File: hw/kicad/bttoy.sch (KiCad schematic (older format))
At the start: 35 parts

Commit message: - more schematic work
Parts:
- gave numbers to parts that had none: 35
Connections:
- net GND: now also R5.2, R6.2, R7.2
- net dgb_led1: now reaches U4.17 (PTB1)
- net dgb_led1: now also D3.1 (K)
- net dbg_led2: now reaches U4.18 (PTB2)
- net dbg_led2: now also D4.1 (K)
- net dbg_led3: now reaches U4.19 (PTA8)
- net dbg_led3: now also D5.1 (K)
- no-connect marks 36 -> 56
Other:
- moved on the sheet: D3, D4, D5, R5, R6, R7, U4

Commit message: - start layout
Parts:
- C1, C4, C5, C6, C7, R1, R2, R3, R4, R5, R6, R7: footprint (none) -> kicadlib:SMD_0603_R
- C2: footprint (none) -> kicadlib:SMD_5X5.2_CAP
- C3: footprint (none) -> kicadlib:SMD_0805_R
- D1: footprint (none) -> kicadlib:SMD_1206_DIODE
- D2, D3, D4, D5: footprint (none) -> kicadlib:SMD_0603_LED
- J1: footprint (none) -> kicadlib:usb_micro_b_smt
- J2: footprint (none) -> kicadlib:HC-07_bluetooth
- J3: footprint (none) -> kicadlib:ARM_10_PIN_SMT
- JP1: footprint (none) -> kicadlib:jmp_small
- L1: footprint (none) -> kicadlib:SMD_4x4_INDUCTOR
- P1, P2, P3, P4, P5: footprint (none) -> kicadlib:TEST_0.100
- SW1: footprint (none) -> kicadlib:TH_APEM_MHSS1105_SPDT
- U1, U2, U3: footprint (none) -> kicadlib:SMD_SOT23-5
- U4: footprint (none) -> kicadlib:SMD_LQFP-32
- U5: footprint (none) -> kicadlib:SMD_SOIC-10NB
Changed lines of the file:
@@
 F 0 "U4" H 6500 2450 60  0000 C CNN
 F 1 "MKL05Z32VLC4" H 6550 2300 60  0000 C CNN
-F 2 "" H 6100 2250 60  0000 C CNN
+F 2 "kicadlib:SMD_LQFP-32" H 6100 2250 60  0001 C CNN
 F 3 "" H 6100 2250 60  0000 C CNN
 	1    6100 2250
@@
 F 0 "U3" H 5350 4000 60  0000 C CNN
 F 1 "MCP73831" H 5350 4600 60  0000 C CNN
-F 2 "" H 5350 4300 60  0000 C CNN
+F 2 "kicadlib:SMD_SOT23-5" H 5350 4300 60  0001 C CNN
 F 3 "" H 5350 4300 60  0000 C CNN
 	1    5350 4300
@@
 F 0 "J1" H 1100 600 60  0000 C CNN
 F 1 "USB-micro-b" H 1100 1850 60  0000 C CNN
-F 2 "" H 1100 1200 60  0000 C CNN
+F 2 "kicadlib:usb_micro_b_smt" H 1100 1200 60  0001 C CNN
 F 3 "" H 1100 1200 60  0000 C CNN
 	1    1100 1200
@@
 F 0 "U1" H 1900 4250 60  0000 C CNN
 F 1 "AAT3221/MIC5504" H 1900 4850 60  0000 C CNN
-F 2 "" H 1900 4450 60  0000 C CNN
+F 2 "kicadlib:SMD_SOT23-5" H 1900 4450 60  0001 C CNN
 F 3 "" H 1900 4450 60  0000 C CNN
 	1    1900 4450
@@
 F 0 "R3" V 4630 4950 40  0000 C CNN
 F 1 "1K" V 4557 4951 40  0000 C CNN
-F 2 "" V 4480 4950 30  0000 C CNN
+F 2 "kicadlib:SMD_0603_R" V 4480 4950 30  0001 C CNN
 F 3 "" H 4550 4950 30  0000 C CNN
 	1    4550 4950
@@
 F 0 "C6" H 4250 4450 40  0000 L CNN
 F 1 "4.7uF" H 4256 4265 40  0000 L CNN
-F 2 "" H 4288 4200 30  0000 C CNN
+F 2 "kicadlib:SMD_0603_R" H 4288 4200 30  0001 C CNN
 F 3 "" H 4250 4350 60  0000 C CNN
 	1    4250 4350
@@
 F 0 "D2" H 4550 4450 50  0000 C CNN
 F 1 "LED" H 4550 4250 50  0000 C CNN
-F 2 "" H 4550 4350 60  0000 C CNN
+F 2 "kicadlib:SMD_0603_LED" H 4550 4350 60  0001 C CNN
 F 3 "" H 4550 4350 60  0000 C CNN
 	1    4550 4350
@@
 F 0 "R4" V 6180 4550 40  0000 C CNN
 F 1 "2K" V 6107 4551 40  0000 C CNN
-F 2 "" V 6030 4550 30  0000 C CNN
+F 2 "kicadlib:SMD_0603_R" V 6030 4550 30  0001 C CNN
 F 3 "" H 6100 4550 30  0000 C CNN
 	1    6100 4550
@@
 F 0 "C7" H 6350 4450 40  0000 L CNN
 F 1 "4.7uF" H 6356 4265 40  0000 L CNN
-F 2 "" H 6388 4200 30  0000 C CNN
+F 2 "kicadlib:SMD_0603_R" H 6388 4200 30  0001 C CNN
 F 3 "" H 6350 4350 60  0000 C CNN
 	1    6350 4350
@@
 F 0 "C1" H 1050 4500 40  0000 L CNN
 F 1 "1uF" H 1056 4315 40  0000 L CNN
-F 2 "" H 1088 4250 30  0000 C CNN
+F 2 "kicadlib:SMD_0603_R" H 1088 4250 30  0001 C CNN
 F 3 "" H 1050 4400 60  0000 C CNN
 	1    1050 4400
@@
 F 0 "C4" H 2750 4500 40  0000 L CNN
 F 1 "1uF" H 2756 4315 40  0000 L CNN
-F 2 "" H 2788 4250 30  0000 C CNN
+F 2 "kicadlib:SMD_0603_R" H 2788 4250 30  0001 C CNN
 F 3 "" H 2750 4400 60  0000 C CNN
 	1    2750 4400
@@
 F 0 "J3" H 9650 450 60  0000 C CNN
 F 1 "ARM_10PIN" H 9650 2100 60  0000 C CNN
-F 2 "" H 9650 1450 60  0000 C CNN
+F 2 "kicadlib:ARM_10_PIN_SMT" H 9650 1450 60  0001 C CNN
 F 3 "" H 9650 1450 60  0000 C CNN
 	1    9650 1450
@@
 F 0 "J2" H 4200 -550 60  0000 C CNN
 F 1 "HC-07_BLUETOOTH" H 3350 1850 60  0000 C CNN
-F 2 "" H 2550 1450 60  0000 C CNN
+F 2 "kicadlib:HC-07_bluetooth" H 2550 1450 60  0001 C CNN
 F 3 "" H 2550 1450 60  0000 C CNN
 	1    2550 1450
@@
 F 0 "U2" H 3000 6350 60  0000 C CNN
 F 1 "MIC2288" H 3000 6950 60  0000 C CNN
-F 2 "" H 3000 6600 60  0000 C CNN
+F 2 "kicadlib:SMD_SOT23-5" H 3000 6600 60  0001 C CNN
 F 3 "" H 3000 6600 60  0000 C CNN
 	1    3000 6650
@@
 F 0 "L1" V 2900 6050 40  0000 C CNN
 F 1 "10uH/650mA (LQH43CN100K03)" V 3100 5600 40  0000 C CNN
-F 2 "" H 2950 6050 60  0000 C CNN
+F 2 "kicadlib:SMD_4x4_INDUCTOR" H 2950 6050 60  0001 C CNN
 F 3 "" H 2950 6050 60  0000 C CNN
 	1    2950 6050
@@
 F 0 "C5" H 3650 6900 40  0000 L CNN
 F 1 "2.2uF/10V" H 3656 6715 40  0000 L CNN
-F 2 "" H 3688 6650 30  0000 C CNN
+F 2 "kicadlib:SMD_0603_R" H 3688 6650 30  0001 C CNN
 F 3 "" H 3650 6800 60  0000 C CNN
 	1    3650 6800
@@
 F 0 "C3" H 1800 6250 40  0000 L CNN
 F 1 "10uF/16V" H 1600 6450 40  0000 L CNN
-F 2 "" H 1788 6200 30  0000 C CNN
+F 2 "kicadlib:SMD_0805_R" H 1788 6200 30  0001 C CNN
 F 3 "" H 1750 6350 60  0000 C CNN
 	1    1750 6350
@@
 F 0 "D1" H 2350 6150 40  0000 C CNN
 F 1 "40v/1A" H 2350 5950 40  0000 C CNN
-F 2 "" H 2350 6050 60  0000 C CNN
+F 2 "kicadlib:SMD_1206_DIODE" H 2350 6050 60  0001 C CNN
 F 3 "" H 2350 6050 60  0000 C CNN
 	1    2350 6050
@@
 F 0 "R1" V 2130 6500 40  0000 C CNN
 F 1 "6.2K" V 2057 6501 40  0000 C CNN
-F 2 "" V 1980 6500 30  0000 C CNN
+F 2 "kicadlib:SMD_0603_R" V 1980 6500 30  0001 C CNN
 F 3 "" H 2050 6500 30  0000 C CNN
 	1    2050 6500
@@
 F 0 "R2" V 2130 7100 40  0000 C CNN
 F 1 "1K" V 2057 7101 40  0000 C CNN
-F 2 "" V 1980 7100 30  0000 C CNN
+F 2 "kicadlib:SMD_0603_R" V 1980 7100 30  0001 C CNN
 F 3 "" H 2050 7100 30  0000 C CNN
 	1    2050 7100
@@
 F 0 "JP1" H 3050 7600 60  0000 C CNN
 F 1 "MPS ENABLE" H 3050 7370 40  0000 C CNN
-F 2 "" H 3050 7450 60  0000 C CNN
+F 2 "kicadlib:jmp_small" H 3050 7450 60  0001 C CNN
 F 3 "" H 3050 7450 60  0000 C CNN
 	1    3050 7450
@@
 F 0 "SW1" H 6900 4300 50  0000 C CNN
 F 1 "SPDT (Apem MHSS1105)" H 7200 3900 50  0000 C CNN
-F 2 "" H 7100 4150 60  0000 C CNN
+F 2 "kicadlib:TH_APEM_MHSS1105_SPDT" H 7100 4150 60  0001 C CNN
 F 3 "" H 7100 4150 60  0000 C CNN
 	1    7100 4150
@@
 F 0 "C2" H 1200 6450 50  0000 L CNN
 F 1 "30uF" H 1150 6250 50  0000 L CNN
-F 2 "" H 1150 6350 60  0000 C CNN
+F 2 "kicadlib:SMD_5X5.2_CAP" H 1150 6350 60  0001 C CNN
 F 3 "" H 1150 6350 60  0000 C CNN
 	1    1150 6350
@@
 F 0 "U5" H 6900 5600 60  0000 C CNN
 F 1 "LV8548" H 6900 6400 60  0000 C CNN
-F 2 "" H 6800 6050 60  0000 C CNN
+F 2 "kicadlib:SMD_SOIC-10NB" H 6800 6050 60  0001 C CNN
 F 3 "" H 6800 6050 60  0000 C CNN
 	1    6900 6050
@@
 F 0 "P2" H 7650 5850 40  0000 C CNN
 F 1 "M1+" H 7650 5800 30  0000 C CNN
-F 2 "" H 7650 5550 60  0000 C CNN
+F 2 "kicadlib:TEST_0.100" H 7650 5550 60  0001 C CNN
 F 3 "" H 7650 5550 60  0000 C CNN
 	1    7650 5550
@@
 F 0 "P3" H 7650 6250 40  0000 C CNN
 F 1 "M1-" H 7650 6200 30  0000 C CNN
-F 2 "" H 7650 5950 60  0000 C CNN
+F 2 "kicadlib:TEST_0.100" H 7650 5950 60  0001 C CNN
 F 3 "" H 7650 5950 60  0000 C CNN
 	1    7650 5950
@@
 F 0 "P4" H 8400 6350 40  0000 C CNN
 F 1 "M2+" H 8400 6300 30  0000 C CNN
-F 2 "" H 8400 6050 60  0000 C CNN
+F 2 "kicadlib:TEST_0.100" H 8400 6050 60  0001 C CNN
 F 3 "" H 8400 6050 60  0000 C CNN
 	1    8400 6050
@@
 F 0 "P5" H 8400 6750 40  0000 C CNN
 F 1 "M2-" H 8400 6700 30  0000 C CNN
-F 2 "" H 8400 6450 60  0000 C CNN
+F 2 "kicadlib:TEST_0.100" H 8400 6450 60  0001 C CNN
 F 3 "" H 8400 6450 60  0000 C CNN
 	1    8400 6450
@@
 F 0 "P1" H 1150 6200 40  0000 C CNN
 F 1 "+9V_DBG" H 1150 6150 30  0000 C CNN
-F 2 "" H 1150 5900 60  0000 C CNN
+F 2 "kicadlib:TEST_0.100" H 1150 5900 60  0001 C CNN
 F 3 "" H 1150 5900 60  0000 C CNN
 	1    1150 5900
@@
 F 0 "D3" H 8700 4000 50  0000 C CNN
 F 1 "LED" H 8700 3800 50  0000 C CNN
-F 2 "" H 8700 3900 60  0000 C CNN
+F 2 "kicadlib:SMD_0603_LED" H 8700 3900 60  0001 C CNN
 F 3 "" H 8700 3900 60  0000 C CNN
 	1    8700 3900
@@
 F 0 "R5" V 8780 4450 40  0000 C CNN
 F 1 "1K" V 8707 4451 40  0000 C CNN
-F 2 "" V 8630 4450 30  0000 C CNN
+F 2 "kicadlib:SMD_0603_R" V 8630 4450 30  0001 C CNN
 F 3 "" H 8700 4450 30  0000 C CNN
 	1    8700 4450
@@
 F 0 "D4" H 9050 4000 50  0000 C CNN
 F 1 "LED" H 9050 3800 50  0000 C CNN
-F 2 "" H 9050 3900 60  0000 C CNN
+F 2 "kicadlib:SMD_0603_LED" H 9050 3900 60  0001 C CNN
 F 3 "" H 9050 3900 60  0000 C CNN
 	1    9050 3900
@@
 F 0 "R6" V 9130 4450 40  0000 C CNN
 F 1 "1K" V 9057 4451 40  0000 C CNN
-F 2 "" V 8980 4450 30  0000 C CNN
+F 2 "kicadlib:SMD_0603_R" V 8980 4450 30  0001 C CNN
 F 3 "" H 9050 4450 30  0000 C CNN
 	1    9050 4450
@@
 F 0 "D5" H 9400 4000 50  0000 C CNN
 F 1 "LED" H 9400 3800 50  0000 C CNN
-F 2 "" H 9400 3900 60  0000 C CNN
+F 2 "kicadlib:SMD_0603_LED" H 9400 3900 60  0001 C CNN
 F 3 "" H 9400 3900 60  0000 C CNN
 	1    9400 3900
@@
 F 0 "R7" V 9480 4450 40  0000 C CNN
 F 1 "1K" V 9407 4451 40  0000 C CNN
-F 2 "" V 9330 4450 30  0000 C CNN
+F 2 "kicadlib:SMD_0603_R" V 9330 4450 30  0001 C CNN
 F 3 "" H 9400 4450 30  0000 C CNN
 	1    9400 4450

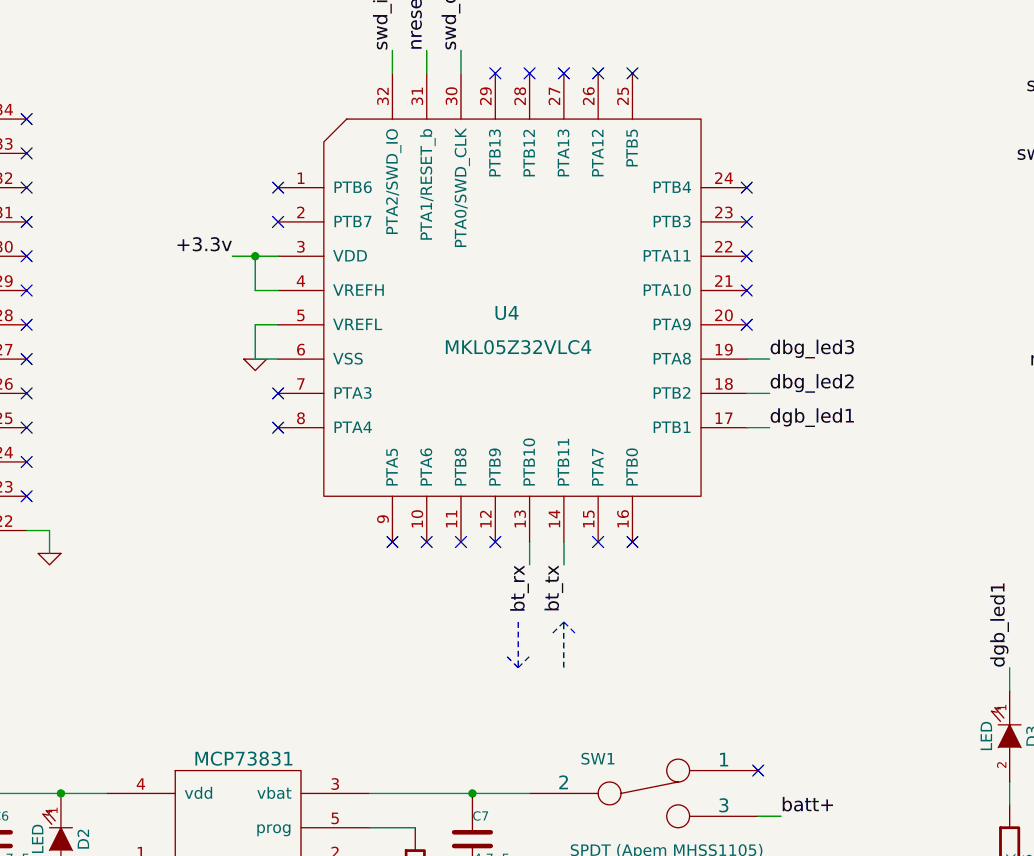
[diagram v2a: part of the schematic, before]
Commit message: - connect motor control signals
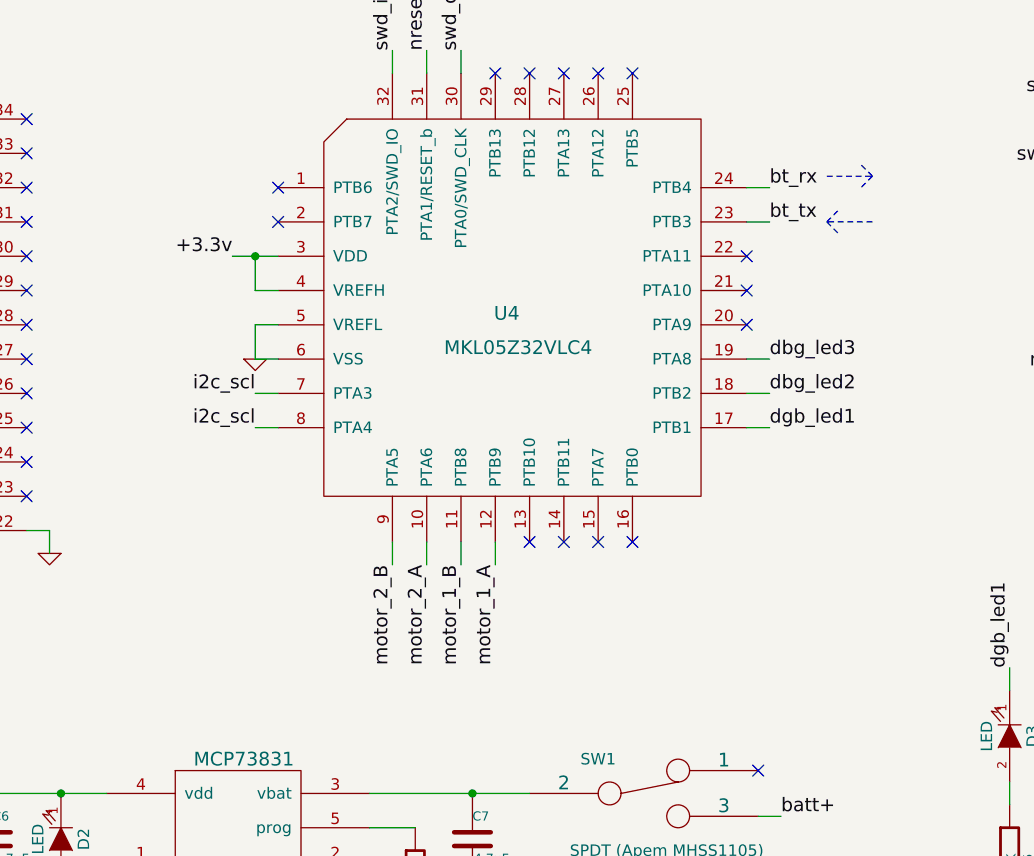
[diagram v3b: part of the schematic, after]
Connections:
- net bt_rx: now also U4.24 (PTB4); no longer U4.13 (PTB10)
- net bt_tx: now also U4.23 (PTB3); no longer U4.14 (PTB11)
- net motor_1_A: now also U4.12 (PTB9)
- net motor_1_B: now also U4.11 (PTB8)
- net motor_2_A: now also U4.10 (PTA6)
- net motor_2_B: now also U4.9 (PTA5)
- net i2c_scl: now reaches U4.7 (PTA3)
- net i2c_scl: now also U4.8 (PTA4)
- no-connect marks 56 -> 50
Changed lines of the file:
@@
 Text Label 2250 1200 2    60   ~ 0
 bt_tx
-Text Label 6600 3150 3    60   ~ 0
+Text Label 7650 1500 0    60   ~ 0
 bt_rx
-Text Label 6750 3150 3    60   ~ 0
+Text Label 7650 1650 0    60   ~ 0
 bt_tx
 Text Label 6300 5950 2    60   ~ 0
@@
 Connection ~ 5400 1800
 Wire Notes Line
-	6550 3400 6550 3600
-Wire Notes Line
-	6550 3600 6600 3550
-Wire Notes Line
-	6550 3600 6500 3550
-Wire Wire Line
-	6600 3150 6600 3050
-Wire Notes Line
-	6750 3600 6750 3400
-Wire Notes Line
-	6750 3400 6700 3450
-Wire Notes Line
-	6750 3400 6800 3450
-Wire Wire Line
-	6750 3150 6750 3050
+	7900 1450 8100 1450
+Wire Notes Line
+	8100 1450 8050 1400
+Wire Notes Line
+	8100 1450 8050 1500
+Wire Notes Line
+	8100 1650 7900 1650
+Wire Notes Line
+	7900 1650 7950 1700
+Wire Notes Line
+	7900 1650 7950 1600
 Wire Wire Line
 	6300 5800 6400 5800
@@
 NoConn ~ 7050 3050
 NoConn ~ 6900 3050
-NoConn ~ 6450 3050
-NoConn ~ 6300 3050
-NoConn ~ 6150 3050
-NoConn ~ 6000 3050
-NoConn ~ 5500 2550
-NoConn ~ 5500 2400
 NoConn ~ 7550 2100
 NoConn ~ 7550 1950
 NoConn ~ 7550 1800
-NoConn ~ 7550 1650
-NoConn ~ 7550 1500
 NoConn ~ 7050 1000
 NoConn ~ 6900 1000
@@
 NoConn ~ 5500 1500
 NoConn ~ 5500 1650
+Text Label 6300 3150 3    60   ~ 0
+motor_1_B
+Text Label 6000 3150 3    60   ~ 0
+motor_2_B
+Wire Wire Line
+	6000 3150 6000 3050
+Wire Wire Line
+	6150 3050 6150 3150
+Text Label 6150 3150 3    60   ~ 0
+motor_2_A
+Text Label 6450 3150 3    60   ~ 0
+motor_1_A
+Wire Wire Line
+	6300 3150 6300 3050
+Wire Wire Line
+	6450 3050 6450 3150
+Text Label 5400 2400 2    60   ~ 0
+i2c_scl
+Text Label 5400 2550 2    60   ~ 0
+i2c_scl
+Wire Wire Line
+	5400 2550 5500 2550
+Wire Wire Line
+	5500 2400 5400 2400
+NoConn ~ 6750 3050
+NoConn ~ 6600 3050
+Wire Wire Line
+	7550 1500 7650 1500
+Wire Wire Line
+	7650 1650 7550 1650
 $EndSCHEMATC
